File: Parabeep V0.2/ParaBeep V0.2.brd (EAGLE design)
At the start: 35.3 x 57.5 mm, 48 parts, among them J1 MICRO-SD_CARD_SOCKETPUSH-PUSH, Q1 500mA/300V, U1 ADXL345, U2 BQ25570RGRR, U3 TPS78330DDCRDDC5_TEX-L, U4 UBLOX_SAM_M8Q-0-10, U5 MS5803-14BA

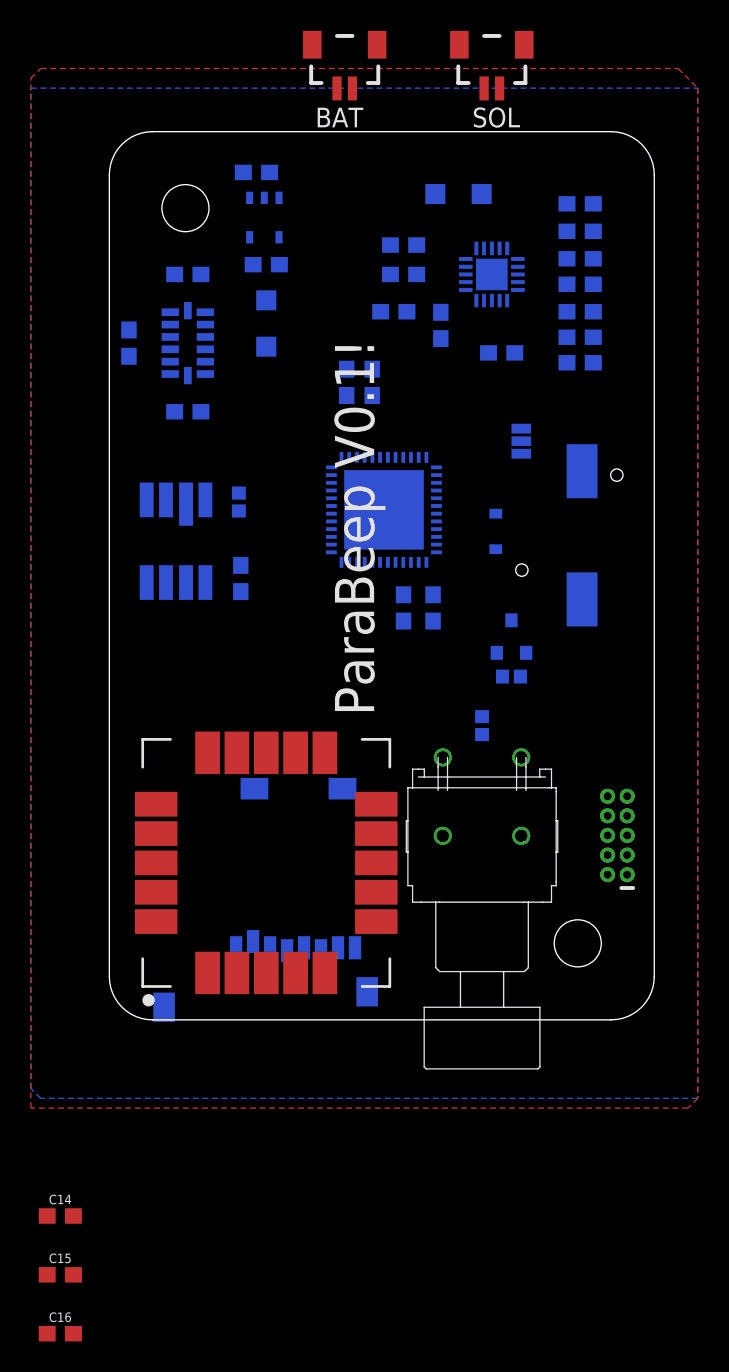
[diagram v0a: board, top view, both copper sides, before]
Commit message: parabeep v0.2 ordered
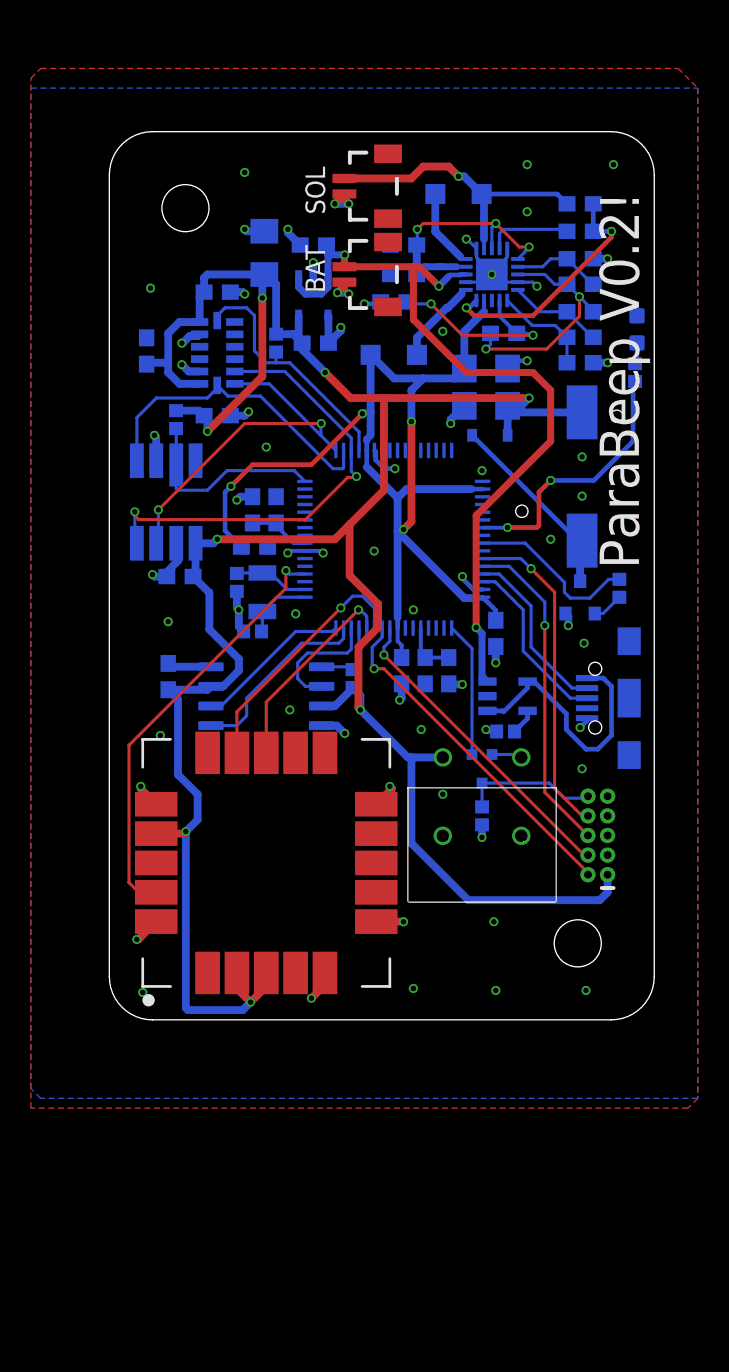
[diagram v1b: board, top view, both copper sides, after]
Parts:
- removed J1: MICRO-SD_CARD_SOCKETPUSH-PUSH, SparkFun-Connectors:MICRO-SD-SOCKET
- removed JP1: JUMPER-SMT_3_NO_SILK, SparkFun-Jumpers:SMT-JUMPER_3_NO_SILK
- added C18: 0.1uF, SparkFun-Capacitors:0603
- added C19, C22: 33uF, SparkFun-Capacitors:1206
- added C20, C21: 6pF, SparkFun-Capacitors:0402
- added D2: GREEN, SparkFun-LED:LED-0603
- added IC2: MCP73811/2, adafruit:SOT23-5L
- added J2: (no value), SparkFun-Connectors:USB-B-MICRO-SMD
- added R11, R12, R25, R8: (no value), SparkFun-Resistors:0402
- added U$2: DMG1013UW-7, DMG1013UW-7:DMG1013UW-7
- added U6: ATSAMD51J20A-A, SparkFun-IC-Microcontroller:TQFP64
- added U7: AT25SF128A-SHB-T, AT25SF128A-SHB-T:SOIC127P790X216-8N
- added Y1: 32.768kHz, SparkFun-Clocks:CRYSTAL-SMD-3.2X1.5MM
- C1: value 4.7uF -> 33uF; device SparkFun-Capacitors:0603 -> SparkFun-Capacitors:1206
- U$5: value ATSAMD51G19A -> (none); device SparkFun-IC-Microcontroller:QFN-48 -> para:PARA
- moved C16 55.1 mm to (10.8, 33.0), flipped to the bottom, turned to 90 degrees
- moved C15 44.9 mm to (18.9, 22.6), flipped to the bottom, turned to 270 degrees
- moved C14 43.3 mm to (22.0, 22.6), flipped to the bottom, turned to 270 degrees
- moved C11 19.3 mm to (20.4, 22.6), turned to 270 degrees
- moved U$5 16.0 mm to (19.7, 17.1), turned to 270 degrees
- moved BAT 14.1 mm to (17.1, 48.3), turned to 90 degrees
- moved L2 12.2 mm to (9.40, 30.6), turned to 180 degrees
- moved C3 11.3 mm to (9.27, 33.0)
- moved SOL 11.2 mm to (17.1, 54.0), turned to 90 degrees
- moved R13 9.03 mm to (33.0, 27.9), turned to 90 degrees
- moved L3 8.50 mm to (18.4, 43.1), turned to 0 degrees
- moved R4 6.71 mm to (4.32, 38.9)
- moved D1 6.23 mm to (24.6, 37.8), turned to 0 degrees
- moved C12 6.19 mm to (25.0, 25.0)
- moved C4 5.99 mm to (13.3, 43.8)
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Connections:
- removed net SC_MEM: J1.CS
- removed net SPI_MISO: J1.DO, U1.12, U5.8
- removed net SPI_MOSI: J1.DI, U1.13, U5.7
- removed net SPI_SCK: J1.SCLK, U1.14, U5.1
- removed net USART_RX: U4.13
- removed net USART_TX: U4.14
- new net CS_MEM: R11.1, U6.61, U7.1
- new net D+: J2.D+, U6.46
- new net D-: J2.D-, U6.45
- new net LED: R12.2, U6.39
- new net N$14: C18.2, U7.8
- new net N$17: D2.A, R12.1
- new net N$18: IC2.5, R25.2
- new net RSTLCK: U$2.1, U6.49
- new net SERCOM0_MISO: U1.12, U5.8, U6.19
- new net SERCOM0_MOSI: U1.13, U5.7, U6.17
- new net SERCOM0_SCK: U1.14, U5.1, U6.18
- new net SERCOM5_MISO: U6.62, U7.2
- new net SERCOM5_MOSI: U6.63, U7.5
- new net SERCOM5_SCK: U6.64, U7.6
- new net SERCOM7_RX: U4.13, U6.60
- new net SERCOM7_TX: U4.14, U6.59
- new net VBUS: IC2.1, IC2.4, J2.VBUS
- net !RESET: now also R5.2, U$2.3
- net BUTTON: now also U$2.2, U$3.P$2; no longer R5.2, U$3.P$1
- net BUZZER: now also U6.41
- net CS_ACCEL: now also R8.1, U6.20
- net CS_BARO: now also U6.16
- net GND: now also C19.2, C20.1, C21.1, C22.2, D2.C, IC2.2, J2.GND, R25.1, SOL.1, U6.22, U6.33, U6.47, U6.54, U6.7, U7.4; no longer SOL.2, U$5.18, U$5.35, U$5.42, U$5.5, U$5.EP
- net GPS_INT: now also U6.4
- net N$1: now also C20.2, U6.1, Y1.P$2; no longer C3.1
- net N$11: now also SOL.2; no longer SOL.1
- net N$19: now also U6.53; no longer U$5.41
- net N$2: now also C21.2, U6.2, Y1.P$1; no longer D1.C, JP1.2, SG1.-
- net N$23: now also C3.1, U6.8; no longer U$5.6
- net RX: now also U6.44
- net SWCLK: now also U6.57
- net SWDIO: now also U6.58
- net TX: now also U6.43
- net VCC-ISO: now also C19.1, U6.21, U6.34, U6.48, U6.56; no longer C1.1, U$5.17, U$5.36, U$5.44
- net VCC_1: now also C1.1, C18.1, C22.1, D1.C, R11.2, R8.2, SG1.-, U$3.P$1, U7.3, U7.7; no longer JP1.3, U$3.P$2
- net VIN: now also IC2.3; no longer JP1.1
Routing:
- net VCC_1: track 0.00 -> 175.5 mm, vias 0 -> 8
- net VCC-ISO: track 0.00 -> 74.6 mm, vias 0 -> 4
- net GND: track 0.00 -> 63.9 mm, vias 0 -> 67
- net VIN: track 0.00 -> 51.7 mm, vias 0 -> 3
- net SERCOM0_MISO: track 0.00 -> 30.4 mm, vias 0 -> 2
- net GPS_INT: track 0.00 -> 27.8 mm, vias 0 -> 1
- net SERCOM0_MOSI: track 0.00 -> 24.3 mm, vias 0 -> 2
- net SWDIO: track 0.00 -> 22.4 mm, vias 0 -> 1
- net RX: track 0.00 -> 21.3 mm, vias 0 -> 1
- net TX: track 0.00 -> 21.2 mm, vias 0 -> 1
- net SERCOM0_SCK: track 0.00 -> 21.0 mm
- net SWCLK: track 0.00 -> 20.5 mm, vias 0 -> 1
- net N$11: track 0.00 -> 19.3 mm, vias 0 -> 1
- net LED: track 0.00 -> 17.2 mm, vias 0 -> 2
- net N$16: track 0.00 -> 17.2 mm, vias 0 -> 3
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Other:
- board text added: "ParaBeep V0.2!"
- board text removed: "ParaBeep V0.1!"

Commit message: parabeep v0.2 order third try
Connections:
- new net EN: U3.3, U6.25
- net VCC-ISO: now also U$3.P$1
- net VCC_1: no longer U$3.P$1
- net VIN: no longer U3.3
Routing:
- net EN: track 0.00 -> 13.9 mm, vias 0 -> 2
- net VCC-ISO: track 74.6 -> 83.3 mm
- net VCC_1: track 175.5 -> 173.4 mm
- net VIN: track 51.7 -> 53.8 mm, vias 3 -> 4
- net GND: track 63.9 -> 63.8 mm, vias 67 -> 66
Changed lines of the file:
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@@
 <wire x1="14.986" y1="44.616" x2="14.986" y2="44.831" width="0.508" layer="16"/>
 <via x="14.986" y="44.831" extent="1-16" drill="0.35"/>
-<wire x1="13.208" y1="48.13935" x2="13.208" y2="49.022" width="0.508" layer="16"/>
-<via x="13.208" y="49.022" extent="1-16" drill="0.35"/>
+<wire x1="13.208" y1="48.13935" x2="13.208" y2="47.371" width="0.508" layer="16"/>
+<via x="13.208" y="47.371" extent="1-16" drill="0.35"/>
 <wire x1="12.358" y1="50.165" x2="11.557" y2="50.966" width="0.508" layer="16"/>
 <wire x1="11.557" y1="50.966" x2="11.557" y2="51.181" width="0.508" layer="16"/>
@@
 <via x="11.684" y="20.066" extent="1-16" drill="0.35"/>
 <via x="3.302" y="18.415" extent="1-16" drill="0.35"/>
-<via x="20.193" y="18.796" extent="1-16" drill="0.35"/>
 <via x="21.59" y="14.605" extent="1-16" drill="0.35"/>
 <via x="30.607" y="16.256" extent="1-16" drill="0.35"/>
@@
 <wire x1="18.165" y1="25.365" x2="18.165" y2="24.515" width="0.2032" layer="16"/>
 <wire x1="18.165" y1="24.515" x2="17.78" y2="24.13" width="0.2032" layer="16"/>
-<wire x1="17.78" y1="24.13" x2="17.78" y2="23.622" width="0.2032" layer="16"/>
-<via x="17.78" y="23.622" extent="1-16" drill="0.35"/>
-<wire x1="17.78" y1="23.622" x2="30.734" y2="10.668" width="0.2032" layer="1"/>
-<wire x1="30.734" y1="10.668" x2="30.988" y2="10.668" width="0.2032" layer="1"/>
+<wire x1="17.78" y1="24.13" x2="17.78" y2="24.003" width="0.2032" layer="16"/>
+<via x="17.78" y="24.003" extent="1-16" drill="0.35"/>
+<wire x1="17.78" y1="24.003" x2="17.78" y2="23.368" width="0.2032" layer="1"/>
+<wire x1="30.48" y1="10.668" x2="17.78" y2="23.368" width="0.2032" layer="1"/>
+<wire x1="30.48" y1="10.668" x2="30.988" y2="10.668" width="0.2032" layer="1"/>
 </signal>
 <signal name="!RESET">
@@
 <contactref element="U7" pad="3"/>
 <contactref element="R11" pad="2"/>
-<contactref element="U$3" pad="P$1"/>
 <contactref element="C1" pad="1"/>
 <wire x1="30.607" y1="39.329" x2="26.206" y2="39.329" width="0.508" layer="16"/>
@@
 <wire x1="10.16" y1="3.035" x2="10.16" y2="2.159" width="0.508" layer="1"/>
 <wire x1="10.16" y1="2.159" x2="9.144" y2="1.143" width="0.508" layer="1"/>
-<wire x1="16.256" y1="20.066" x2="19.3294" y2="16.9926" width="0.508" layer="16"/>
-<wire x1="19.3294" y1="16.9926" x2="19.558" y2="16.9926" width="0.508" layer="16"/>
-<wire x1="19.558" y1="16.9926" x2="21.59" y2="16.9926" width="0.508" layer="16"/>
+<wire x1="16.256" y1="20.066" x2="19.558" y2="16.764" width="0.508" layer="16"/>
 <wire x1="32.258" y1="9.398" x2="32.258" y2="8.255" width="0.508" layer="16"/>
 <wire x1="32.258" y1="8.255" x2="31.75" y2="7.747" width="0.508" layer="16"/>
 <wire x1="31.75" y1="7.747" x2="23.241" y2="7.747" width="0.508" layer="16"/>
-<wire x1="19.558" y1="11.43" x2="19.558" y2="16.9926" width="0.508" layer="16"/>
+<wire x1="19.558" y1="11.43" x2="19.558" y2="16.764" width="0.508" layer="16"/>
 <wire x1="23.241" y1="7.747" x2="19.558" y2="11.43" width="0.508" layer="16"/>
 </signal>
 <signal name="VIN">
 <contactref element="U3" pad="1"/>
-<contactref element="U3" pad="3"/>
 <contactref element="C5" pad="1"/>
 <contactref element="U2" pad="18"/>
 <contactref element="BAT" pad="2"/>
-<wire x1="14.158" y1="48.13935" x2="14.158" y2="47.432" width="0.4572" layer="16"/>
-<wire x1="14.158" y1="47.432" x2="13.716" y2="46.99" width="0.4572" layer="16"/>
-<wire x1="13.716" y1="46.99" x2="12.7" y2="46.99" width="0.4572" layer="16"/>
-<wire x1="12.7" y1="46.99" x2="12.258" y2="47.432" width="0.4572" layer="16"/>
 <wire x1="12.258" y1="47.432" x2="12.258" y2="48.13935" width="0.4572" layer="16"/>
 <wire x1="14.058" y1="50.165" x2="14.158" y2="50.065" width="0.4572" layer="16"/>
 <wire x1="14.158" y1="50.065" x2="14.158" y2="49.53" width="0.4572" layer="16"/>
-<wire x1="14.158" y1="49.53" x2="14.158" y2="48.13935" width="0.4572" layer="16"/>
 <wire x1="15.22" y1="48.76" x2="15.22" y2="49.51" width="0.4572" layer="1"/>
 <wire x1="15.22" y1="49.51" x2="15.24" y2="49.53" width="0.4572" layer="1"/>
@@
 <wire x1="28.575" y1="40.767" x2="28.575" y2="37.465" width="0.4572" layer="1"/>
 <wire x1="28.575" y1="37.465" x2="23.749" y2="32.639" width="0.4572" layer="1"/>
+<wire x1="12.258" y1="48.13935" x2="12.258" y2="48.453" width="0.508" layer="16"/>
+<wire x1="13.0636" y1="49.2586" x2="13.0763375" y2="49.2586" width="0.508" layer="16"/>
+<wire x1="13.8827375" y1="50.065" x2="14.158" y2="50.065" width="0.508" layer="16"/>
+<wire x1="13.0763375" y1="49.2586" x2="13.59536875" y2="49.77763125" width="0.508" layer="16"/>
+<wire x1="13.59536875" y1="49.77763125" x2="13.8827375" y2="50.065" width="0.508" layer="16"/>
+<wire x1="12.258" y1="48.453" x2="13.0636" y2="49.2586" width="0.508" layer="16"/>
+<wire x1="15.22" y1="48.76" x2="14.831" y2="49.149" width="0.508" layer="1"/>
+<wire x1="14.831" y1="49.149" x2="13.716" y2="49.149" width="0.508" layer="1"/>
+<via x="13.716" y="49.149" extent="1-16" drill="0.35"/>
+<wire x1="13.716" y1="49.149" x2="13.1859375" y2="49.149" width="0.508" layer="16"/>
+<wire x1="13.1859375" y1="49.149" x2="13.0763375" y2="49.2586" width="0.508" layer="16"/>
+<wire x1="13.716" y1="49.149" x2="14.097" y2="49.53" width="0.508" layer="16"/>
+<wire x1="14.097" y1="49.53" x2="14.158" y2="49.53" width="0.508" layer="16"/>
+<wire x1="13.716" y1="49.149" x2="13.716" y2="49.657" width="0.508" layer="16"/>
+<wire x1="13.716" y1="49.657" x2="13.59536875" y2="49.77763125" width="0.508" layer="16"/>
 </signal>
 <signal name="N$10">
@@
 <wire x1="7.493" y1="31.662" x2="7.493" y2="34.163" width="0.3048" layer="16"/>
 <wire x1="9.271" y1="35.941" x2="13.081" y2="35.941" width="0.3048" layer="1"/>
+<contactref element="U$3" pad="P$1"/>
+<wire x1="18.923" y1="23.456" x2="17.907" y2="22.44" width="0.254" layer="16"/>
+<wire x1="21.1074" y1="16.9926" x2="21.59" y2="16.9926" width="0.254" layer="16"/>
+<wire x1="17.907" y1="22.44" x2="17.907" y2="20.193" width="0.254" layer="16"/>
+<wire x1="17.907" y1="20.193" x2="21.1074" y2="16.9926" width="0.254" layer="16"/>
 </signal>
 <signal name="N$19">
@@
 <wire x1="25.769" y1="31.865" x2="25.781" y2="31.877" width="0.254" layer="16"/>
 </signal>
+<signal name="EN">
+<contactref element="U6" pad="25"/>
+<contactref element="U3" pad="3"/>
+<wire x1="18.665" y1="36.865" x2="18.665" y2="40.136" width="0.254" layer="16"/>
+<wire x1="18.665" y1="40.136" x2="17.78" y2="41.021" width="0.254" layer="16"/>
+<via x="17.78" y="41.021" extent="1-16" drill="0.35"/>
+<wire x1="17.78" y1="41.021" x2="13.843" y2="44.958" width="0.254" layer="1"/>
+<wire x1="13.843" y1="44.958" x2="13.716" y2="45.085" width="0.254" layer="1"/>
+<wire x1="14.158" y1="48.13935" x2="14.158" y2="47.305" width="0.254" layer="16"/>
+<wire x1="14.158" y1="47.305" x2="13.208" y2="46.355" width="0.254" layer="16"/>
+<via x="13.208" y="46.355" extent="1-16" drill="0.35"/>
+<wire x1="13.716" y1="45.085" x2="13.208" y2="45.593" width="0.254" layer="1"/>
+<wire x1="13.208" y1="45.593" x2="13.208" y2="46.355" width="0.254" layer="1"/>
+</signal>
 </signals>

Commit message: working on parabeep v0.2, accel not working yet
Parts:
- R10: value 4.42M -> 3.32M
- R2: value 5.65M -> 4.42M
- R7: value 4.42M -> 6.19M
- R9: value 5.65M -> .549M
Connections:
- net !RESET: now also U6.52
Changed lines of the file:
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@@
 <attribute name="VALUE" x="18.415" y="45.72" size="0.6096" layer="28" font="vector" ratio="20" rot="MR0" align="top-center"/>
 </element>
-<element name="R7" library="SparkFun-Resistors" package="0603" value="4.42M" x="30.48" y="44.196" smashed="yes" rot="MR0">
+<element name="R7" library="SparkFun-Resistors" package="0603" value="6.19M" x="30.48" y="44.196" smashed="yes" rot="MR0">
 <attribute name="NAME" x="32.385" y="44.45" size="0.6096" layer="26" font="vector" ratio="20" rot="MR180" align="bottom-center"/>
 <attribute name="PROD_ID" value=" " x="30.48" y="44.196" size="1.778" layer="28" rot="MR0" display="off"/>
 <attribute name="VALUE" x="30.48" y="43.434" size="0.6096" layer="28" font="vector" ratio="20" rot="MR0" align="top-center"/>
 </element>
-<element name="R9" library="SparkFun-Resistors" package="0603" value="5.65M" x="30.48" y="45.847" smashed="yes" rot="MR0">
+<element name="R9" library="SparkFun-Resistors" package="0603" value=".549M" x="30.48" y="45.847" smashed="yes" rot="MR0">
 <attribute name="NAME" x="32.512" y="46.101" size="0.6096" layer="26" font="vector" ratio="20" rot="MR180" align="bottom-center"/>
 <attribute name="PROD_ID" value=" " x="30.48" y="45.847" size="1.778" layer="28" rot="MR0" display="off"/>
@@
 <attribute name="VALUE" x="30.48" y="48.387" size="0.6096" layer="28" font="vector" ratio="20" rot="MR180" align="top-center"/>
 </element>
-<element name="R2" library="SparkFun-Resistors" package="0603" value="5.65M" x="30.48" y="49.276" smashed="yes" rot="MR180">
+<element name="R2" library="SparkFun-Resistors" package="0603" value="4.42M" x="30.48" y="49.276" smashed="yes" rot="MR180">
 <attribute name="NAME" x="32.639" y="49.53" size="0.6096" layer="26" font="vector" ratio="20" rot="MR180" align="bottom-center"/>
 <attribute name="PROD_ID" value=" " x="30.48" y="49.276" size="1.778" layer="28" rot="MR180" display="off"/>
 <attribute name="VALUE" x="30.48" y="50.038" size="0.6096" layer="28" font="vector" ratio="20" rot="MR180" align="top-center"/>
 </element>
-<element name="R10" library="SparkFun-Resistors" package="0603" value="4.42M" x="30.48" y="42.545" smashed="yes" rot="MR180">
+<element name="R10" library="SparkFun-Resistors" package="0603" value="3.32M" x="30.48" y="42.545" smashed="yes" rot="MR180">
 <attribute name="NAME" x="30.48" y="41.91" size="0.6096" layer="26" font="vector" ratio="20" rot="MR180" align="bottom-center"/>
 <attribute name="PROD_ID" value=" " x="30.48" y="42.545" size="1.778" layer="28" rot="MR180" display="off"/>
@@
 <wire x1="29.464" y1="14.351" x2="30.861" y2="14.351" width="0.2032" layer="16"/>
 <wire x1="30.861" y1="14.351" x2="30.988" y2="14.478" width="0.2032" layer="16"/>
+<contactref element="U6" pad="52"/>
+<wire x1="24.13" y1="15.331" x2="20.665" y2="25.365" width="0" layer="19" extent="16-16"/>
 </signal>
 <signal name="TX">
